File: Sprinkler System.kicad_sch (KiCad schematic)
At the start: 70 parts, among them J1 Main Supply, J2 XFMR_Out, J20 Station_0, J21 Station_1, J22 Station_2, J23 Station_3, J24 Station_4, J25 Station_5, J3 XFMR_In, J4 Conn_Button, J5 UART0, J6 I2C, K1 G3MB-202P, K20 G5LE-1-DC5, K21 G5LE-1-DC5, K22 G5LE-1-DC5, K23 G5LE-1-DC5, K24 G5LE-1-DC5, K25 G5LE-1-DC5, SW1 EN, SW2 BOOT, U1 AMS1117-3.3, U2 EL817, U3 HLK-PM01, U4 ESP32-WROOM-32U, U5 ULN2803A

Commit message: Replace J1 mains connector with 5.08mm MSTBA (250V rated)
The previous Phoenix MC 1,5/3-G-3.81 connector is only rated 160V and
its 3.81mm pitch leaves just 2.0mm Live-to-Earth creepage at 240VAC.
Swap to MSTBA 2,5/3-G-5,08 (project-lib copy with silkscreen clipped at
the board edge), shift J1 up 2.5mm so the deeper body stays flush with
the edge, re-route the L_Supply/Neut/GND stubs, move the E/L/N labels
to the new pad pitch, and reshape the mains demarcation silk line and
the 24V_Comm corner to preserve >=3mm mains-to-SELV spacing.

ERC/DRC: 0 violations.

Co-Authored-By: Claude Fable 5 <noreply@anthropic.com>
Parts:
- J1: footprint Connector_Phoenix_MC:PhoenixContact_MC_1,5_3-G-3.81_1x03_P3.81mm_Horizontal -> Sprinkler System:PhoenixContact_MSTBA_2,5_3-G-5,08_1x03_P5.08mm_Horizontal_EdgeClip
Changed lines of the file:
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@@
 			)
 		)
-		(property "Footprint" "Connector_Phoenix_MC:PhoenixContact_MC_1,5_3-G-3.81_1x03_P3.81mm_Horizontal"
+		(property "Footprint" "Sprinkler System:PhoenixContact_MSTBA_2,5_3-G-5,08_1x03_P5.08mm_Horizontal_EdgeClip"
 			(at 20.32 29.21 0)
 			(hide yes)

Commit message: Add 10D471K MOVs: RV1 across transformer primary, RV2 across mains input
The G3MB-202P SSR has a built-in snubber but no overvoltage element;
Omron requires external overvoltage protection for inductive loads.
RV1 (L_SW-Neut) clamps the transformer-primary inductive kick at J2;
RV2 (L-Neut, after F1) provides the HLK-PM01 datasheet-recommended
line surge protection.

Layout: J2 moved up 4.5mm to open space for RV1 below it (clear of the
H3 mounting hole), earth track jogged from x82 to x82.5 to keep >=3mm
from RV2's Neutral pad, J2's L/N silk labels and Reference/Value moved
with it, F1 reference relocated out of RV2's outline. RV1 uses a
project-library footprint copy with silk clipped at the left to clear
the board-margin line.

ERC/DRC: 0 violations. Mains-to-SELV spacing verified >=3mm.

Co-Authored-By: Claude Fable 5 <noreply@anthropic.com>
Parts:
- added RV1: 10D471K, Sprinkler System:RV_Disc_D12mm_W3.9mm_P7.5mm_EdgeClip, symbol Device:Varistor
- added RV2: 10D471K, Varistor:RV_Disc_D12mm_W3.9mm_P7.5mm, symbol Device:Varistor
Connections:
- net L: now also RV2.1
- net L_SW: now also RV1.1
- net Neut: now also RV1.2, RV2.2

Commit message: Add C5 100nF reset capacitor on ESP32 EN
Espressif's reference design calls for an RC delay on EN (R3 10k was
already present, the capacitor was missing) to guarantee clean power-on
reset as the 3V3 rail rises. Placed beside U4's EN pin, grounded via
the existing GND via at (134.4, 57.8). Also debounces SW1.

ERC/DRC: 0 violations.

Co-Authored-By: Claude Fable 5 <noreply@anthropic.com>
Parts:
- added C5: 100n, Capacitor_SMD:C_0805_2012Metric_Pad1.18x1.45mm_HandSolder, symbol Device:C_Small
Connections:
- net EN: now also C5.1
- net GND: now also C5.2
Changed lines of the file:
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@@
+		)
+	)
+	(symbol
+		(lib_id "Device:C_Small")
+		(at 62.23 139.7 0)
+		(unit 1)
+		(body_style 1)
+		(exclude_from_sim no)
+		(in_bom yes)
+		(on_board yes)
+		(in_pos_files yes)
+		(dnp no)
+		(fields_autoplaced yes)
+		(property "Reference" "C5"
+			(at 64.77 138.42999999999998 0)
+			(show_name no)
+			(do_not_autoplace no)
+			(effects
+				(font
+					(size 1.27 1.27)
+				)
+				(justify left)
+			)
+		)
+		(property "Value" "100n"
+			(at 64.77 140.97 0)
+			(show_name no)
+			(do_not_autoplace no)
+			(effects
+				(font
+					(size 1.27 1.27)
+				)
+				(justify left)
+			)
+		)
+		(property "Footprint" "Capacitor_SMD:C_0805_2012Metric_Pad1.18x1.45mm_HandSolder"
+			(at 62.23 139.7 0)
+			(hide yes)
+			(show_name no)
+			(do_not_autoplace no)
+			(effects
+				(font
+					(size 1.27 1.27)
+				)
+			)
+		)
+		(property "Datasheet" ""
+			(at 62.23 139.7 0)
+			(hide yes)
+			(show_name no)
+			(do_not_autoplace no)
+			(effects
+				(font
+					(size 1.27 1.27)
+				)
+			)
+		)
+		(property "Description" "ESP32 EN reset capacitor"
+			(at 62.23 139.7 0)
+			(hide yes)
+			(show_name no)
+			(do_not_autoplace no)
+			(effects
+				(font
+					(size 1.27 1.27)
+				)
+			)
+		)
+		(pin "1"
+		)
+		(pin "2"
+		)
+		(instances
+			(project "Sprinkler System"
+				(path "/8fa12040-b3d8-4f13-b02e-6c4ba5cdd128"
+					(reference "C5")
+					(unit 1)
+				)
+			)
+		)
+	)
+	(symbol
+		(lib_id "power:GND")
+		(at 62.23 142.23999999999998 0)
+		(unit 1)
+		(body_style 1)
+		(exclude_from_sim no)
+		(in_bom yes)
+		(on_board yes)
+		(in_pos_files yes)
+		(dnp no)
+		(fields_autoplaced yes)
+		(property "Reference" "#PWR084"
+			(at 62.23 142.23999999999998 0)
+			(hide yes)
+			(show_name no)
+			(do_not_autoplace no)
+			(effects
+				(font
+					(size 1.27 1.27)
+				)
+			)
+		)
+		(property "Value" "GND"
+			(at 62.23 148.58999999999997 0)
+			(show_name no)
+			(do_not_autoplace no)
+			(effects
+				(font
+					(size 1.27 1.27)
+				)
+			)
+		)
+		(property "Footprint" ""
+			(at 62.23 142.23999999999998 0)
+			(hide yes)
+			(show_name no)
+			(do_not_autoplace no)
+			(effects
+				(font
+					(size 1.27 1.27)
+				)
+			)
+		)
+		(property "Datasheet" ""
+			(at 62.23 142.23999999999998 0)
+			(hide yes)
+			(show_name no)
+			(do_not_autoplace no)
+			(effects
+				(font
+					(size 1.27 1.27)
+				)
+			)
+		)
+		(property "Description" "Power symbol creates a global label with name \"GND\""
+			(at 62.23 142.23999999999998 0)
+			(hide yes)
+			(show_name no)
+			(do_not_autoplace no)
+			(effects
+				(font
+					(size 1.27 1.27)
+				)
+			)
+		)
+		(pin "1"
+		)
+		(instances
+			(project "Sprinkler System"
+				(path "/8fa12040-b3d8-4f13-b02e-6c4ba5cdd128"
+					(reference "#PWR084")
+					(unit 1)
+				)
+			)
+		)
+	)
+	(wire
+		(pts
+			(xy 62.23 135.89) (xy 62.23 137.16)
+		)
+		(stroke
+			(width 0)
+			(type default)
+		)
+	)
+	(label "EN"
+		(at 62.23 135.89 90)
+		(effects
+			(font
+				(size 1.27 1.27)
+			)
+			(justify left bottom)
 		)
 	)

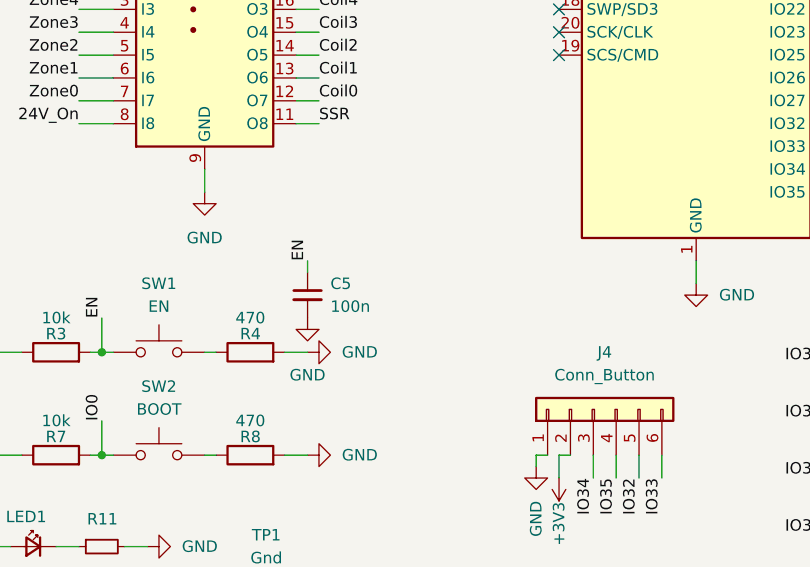
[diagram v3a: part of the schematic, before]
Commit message: Add C6 100nF at ESP32 VDD and C7 220uF bulk on the 5V rail
The HLK-PM01 is rated 600mA and ESP32 WiFi TX bursts approach 500mA;
the 5V rail previously had only 10uF of bulk. C7 (220uF radial, THT
D6.3/P2.5) sits above U3 tapping the +5V/GND module pins on B.Cu with
a via to the existing front-side GND run. C6 gives U4 local 3V3
decoupling next to its VDD pin (none existed within 20mm).

The planned third 100nF at U5 was dropped: every approach to the
ULN2803A's COM/GND pins is walled by the zone-driver fan-out on both
layers, and the ULN has no supply pin proper - the flyback return path
through the 5V artery is already served by C7.

ERC/DRC: 0 violations.

Co-Authored-By: Claude Fable 5 <noreply@anthropic.com>
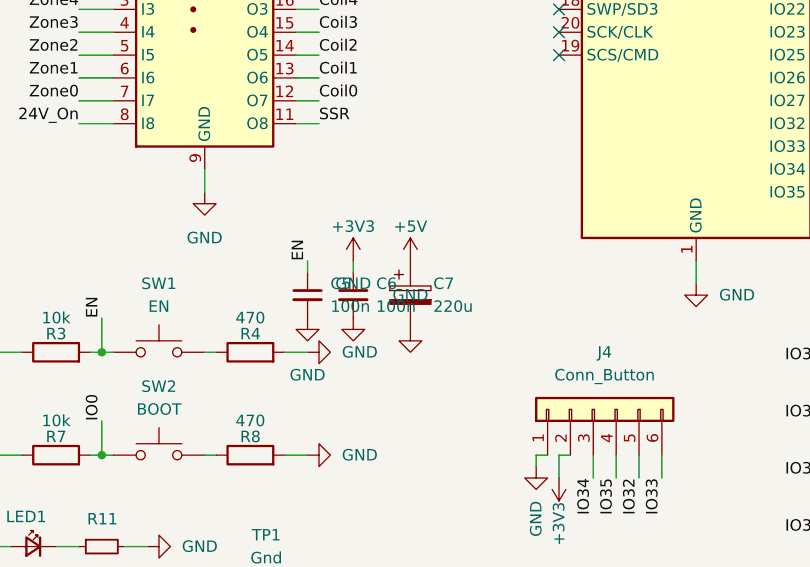
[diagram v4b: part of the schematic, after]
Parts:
- added C6: 100n, Capacitor_SMD:C_0805_2012Metric_Pad1.18x1.45mm_HandSolder, symbol Device:C_Small
- added C7: 220u, Capacitor_THT:CP_Radial_D6.3mm_P2.50mm, symbol Device:C_Polarized
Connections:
- net +3V3: now also C6.1
- net +5V: now also C7.1
- net GND: now also C6.2, C7.2

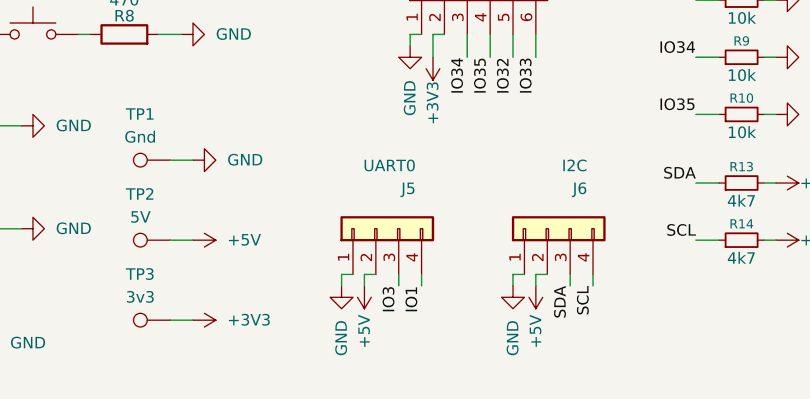
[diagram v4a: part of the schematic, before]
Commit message: Add D2 back-feed blocking diode for the UART/I2C 5V branch (DNP)
SS34 Schottky (SMA, back side) inline in the 5V rail between the main
supply and the J5/J6 connector branch, so an external USB-UART adapter
on J5 can power the board but the HLK-PM01 can never back-drive the
adapter. Marked DNP: bridge the pads (back-side silk note) until a
Schottky is sourced - a plain silicon diode drops too much for the
AMS1117's headroom and must not be substituted.

The branch becomes net +5V_UART (J5 pin 2 and, until the I2C supply
jumper lands in the next change, J6 pin 2). Zones refilled via
kicad-cli --refill-zones.

ERC/DRC: 0 violations.

Co-Authored-By: Claude Fable 5 <noreply@anthropic.com>
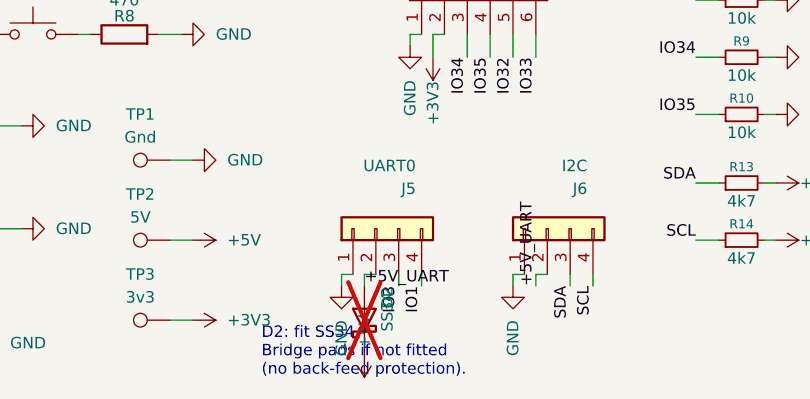
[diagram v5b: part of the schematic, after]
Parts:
- added D2: SS34, Diode_SMD:D_SMA, symbol Device:D_Schottky
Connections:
- net +5V: now also D2.1 (K); no longer J5.2 (Pin_2), J6.2 (Pin_2)
- new net +5V_UART: D2.2 (A), J5.2 (Pin_2), J6.2 (Pin_2)
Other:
- note added: "D2: fit SS34. Bridge pads if not fitted (no back-feed protection)."
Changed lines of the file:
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@@
 	(symbol
 		(lib_id "power:+5V")
-		(at 82.55 185.42 180)
+		(at 82.55 193.04 180)
 		(unit 1)
 		(body_style 1)
@@
 		(dnp no)
 		(property "Reference" "#PWR026"
-			(at 82.55 181.61 0)
+			(at 82.55 189.23 0)
 			(hide yes)
 			(show_name no)
@@
 		)
 		(property "Footprint" ""
-			(at 82.55 185.42 0)
+			(at 82.55 193.04 0)
 			(hide yes)
 			(show_name no)
@@
 		)
 		(property "Datasheet" ""
-			(at 82.55 185.42 0)
+			(at 82.55 193.04 0)
 			(hide yes)
 			(show_name no)
@@
 		)
 		(property "Description" "Power symbol creates a global label with name \"+5V\""
-			(at 82.55 185.42 0)
+			(at 82.55 193.04 0)
 			(hide yes)
 			(show_name no)
@@
 	)
 	(symbol
-		(lib_id "power:+5V")
-		(at 101.6 185.42 180)
-		(unit 1)
-		(body_style 1)
-		(exclude_from_sim no)
-		(in_bom yes)
-		(on_board yes)
-		(in_pos_files yes)
-		(dnp no)
-		(property "Reference" "#PWR025"
-			(at 101.6 181.61 0)
-			(hide yes)
-			(show_name no)
-			(do_not_autoplace no)
-			(effects
-				(font
-					(size 1.27 1.27)
-				)
-			)
-		)
-		(property "Value" "+5V"
-			(at 101.6 190.5 90)
-			(show_name no)
-			(do_not_autoplace no)
-			(effects
-				(font
-					(size 1.27 1.27)
-				)
-			)
-		)
-		(property "Footprint" ""
-			(at 101.6 185.42 0)
-			(hide yes)
-			(show_name no)
-			(do_not_autoplace no)
-			(effects
-				(font
-					(size 1.27 1.27)
-				)
-			)
-		)
-		(property "Datasheet" ""
-			(at 101.6 185.42 0)
-			(hide yes)
-			(show_name no)
-			(do_not_autoplace no)
-			(effects
-				(font
-					(size 1.27 1.27)
-				)
-			)
-		)
-		(property "Description" "Power symbol creates a global label with name \"+5V\""
-			(at 101.6 185.42 0)
-			(hide yes)
-			(show_name no)
-			(do_not_autoplace no)
-			(effects
-				(font
-					(size 1.27 1.27)
-				)
-			)
-		)
-		(pin "1"
-		)
-		(instances
-			(project "Sprinkler System"
-				(path "/8fa12040-b3d8-4f13-b02e-6c4ba5cdd128"
-					(reference "#PWR025")
-					(unit 1)
-				)
-			)
-		)
-	)
-	(symbol
 		(lib_name "R_Small_1")
 		(lib_id "Device:R_Small")
@@
 		)
 	)
+	(symbol
+		(lib_id "Device:D_Schottky")
+		(at 82.55 189.23 90)
+		(unit 1)
+		(body_style 1)
+		(exclude_from_sim no)
+		(in_bom yes)
+		(on_board yes)
+		(in_pos_files yes)
+		(dnp yes)
+		(fields_autoplaced yes)
+		(property "Reference" "D2"
+			(at 85.09 187.95999999999998 0)
+			(show_name no)
+			(do_not_autoplace no)
+			(effects
+				(font
+					(size 1.27 1.27)
+				)
+				(justify left)
+			)
+		)
+		(property "Value" "SS34"
+			(at 85.09 190.5 0)
+			(show_name no)
+			(do_not_autoplace no)
+			(effects
+				(font
+					(size 1.27 1.27)
+				)
+				(justify left)
+			)
+		)
+		(property "Footprint" "Diode_SMD:D_SMA"
+			(at 82.55 189.23 0)
+			(hide yes)
+			(show_name no)
+			(do_not_autoplace no)
+			(effects
+				(font
+					(size 1.27 1.27)
+				)
+			)
+		)
+		(property "Datasheet" ""
+			(at 82.55 189.23 0)
+			(hide yes)
+			(show_name no)
+			(do_not_autoplace no)
+			(effects
+				(font
+					(size 1.27 1.27)
+				)
+			)
+		)
+		(property "Description" "UART 5V back-feed blocking diode. DNP: bridge pads if not fitted."
+			(at 82.55 189.23 0)
+			(hide yes)
+			(show_name no)
+			(do_not_autoplace no)
+			(effects
+				(font
+					(size 1.27 1.27)
+				)
+			)
+		)
+		(pin "1"
+		)
+		(pin "2"
+		)
+		(instances
+			(project "Sprinkler System"
+				(path "/8fa12040-b3d8-4f13-b02e-6c4ba5cdd128"
+					(reference "D2")
+					(unit 1)
+				)
+			)
+		)
+	)
+	(label "+5V_UART"
+		(at 82.55 185.42 0)
+		(effects
+			(font
+				(size 1.27 1.27)
+			)
+			(justify left bottom)
+		)
+	)
+	(label "+5V_UART"
+		(at 101.6 185.42 90)
+		(effects
+			(font
+				(size 1.27 1.27)
+			)
+			(justify left bottom)
+		)
+	)
+	(text "D2: fit SS34.\nBridge pads if not fitted\n(no back-feed protection)."
+		(exclude_from_sim no)
+		(at 71.12 195.58 0)
+		(effects
+			(font
+				(size 1.27 1.27)
+			)
+			(justify left bottom)
+		)
+	)
